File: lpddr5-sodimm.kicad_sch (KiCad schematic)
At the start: 0 parts

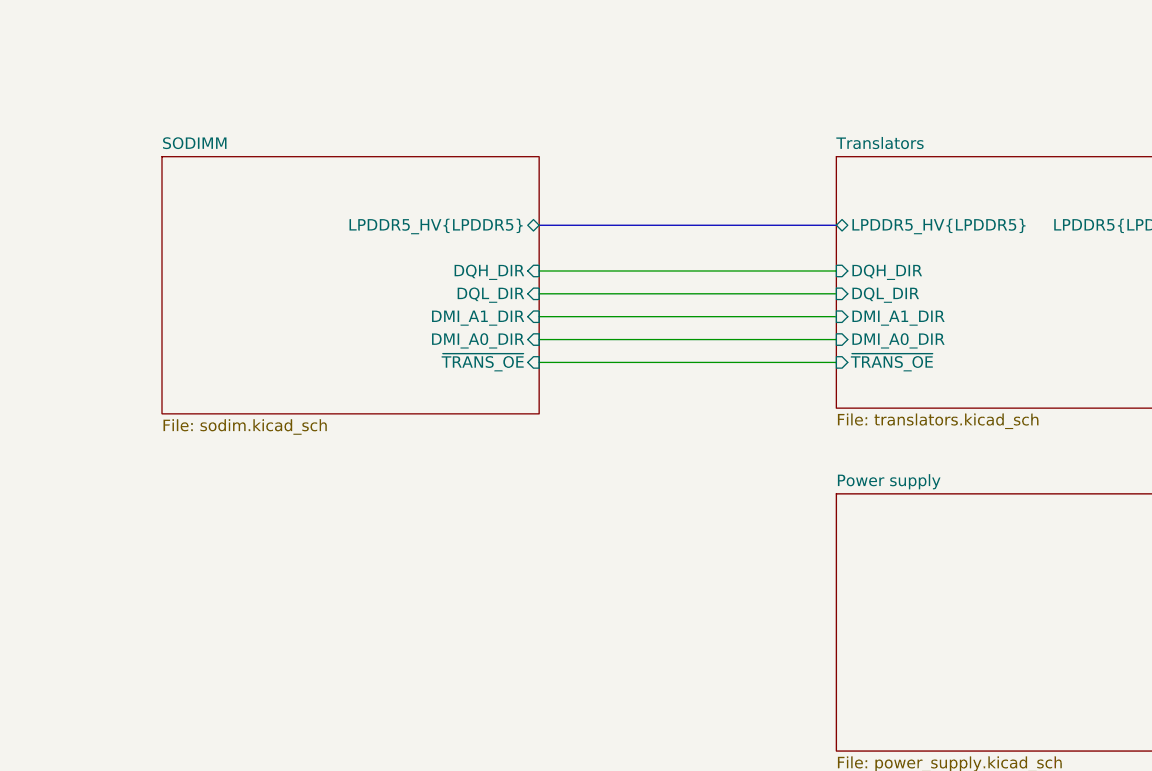
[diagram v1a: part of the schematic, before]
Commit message: [#52835] schematics: connect I2C on root sheet
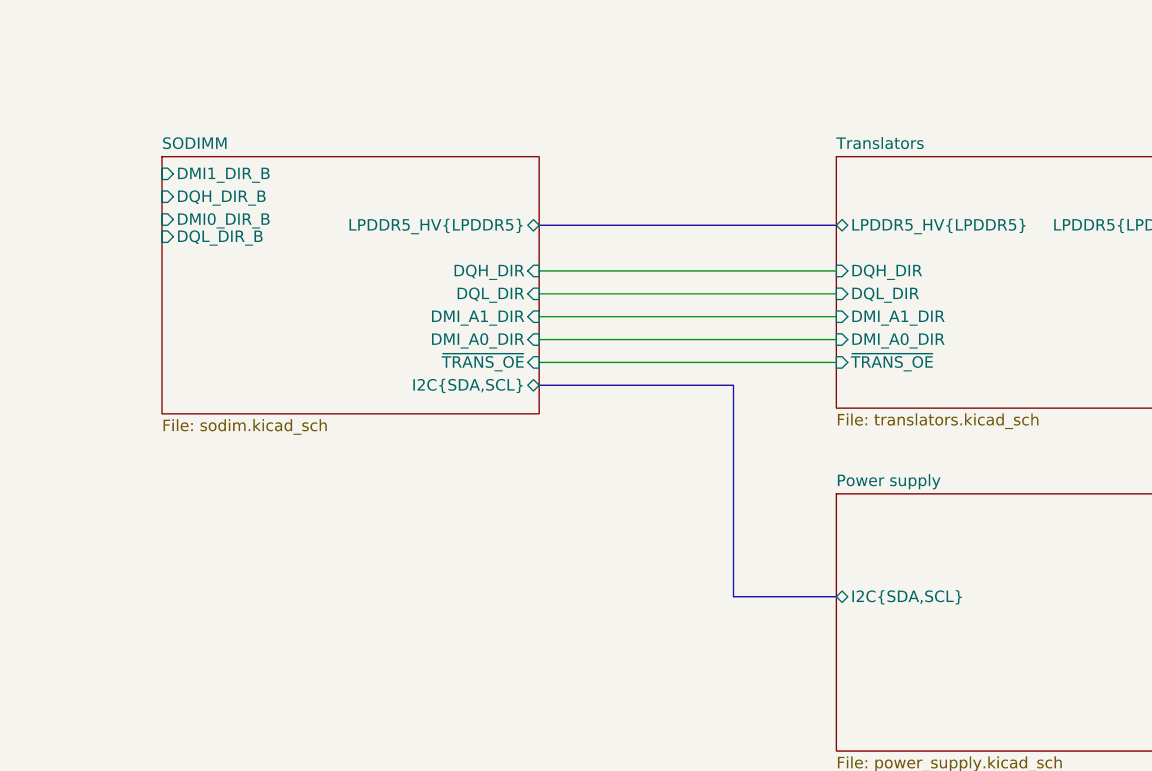
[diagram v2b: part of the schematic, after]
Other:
- sheet Power supply ports: added I2C{SDA,SCL}; removed none
- sheet SODIMM ports: added DMI0_DIR_B, DMI1_DIR_B, DQH_DIR_B, DQL_DIR_B, I2C{SDA,SCL}; removed none

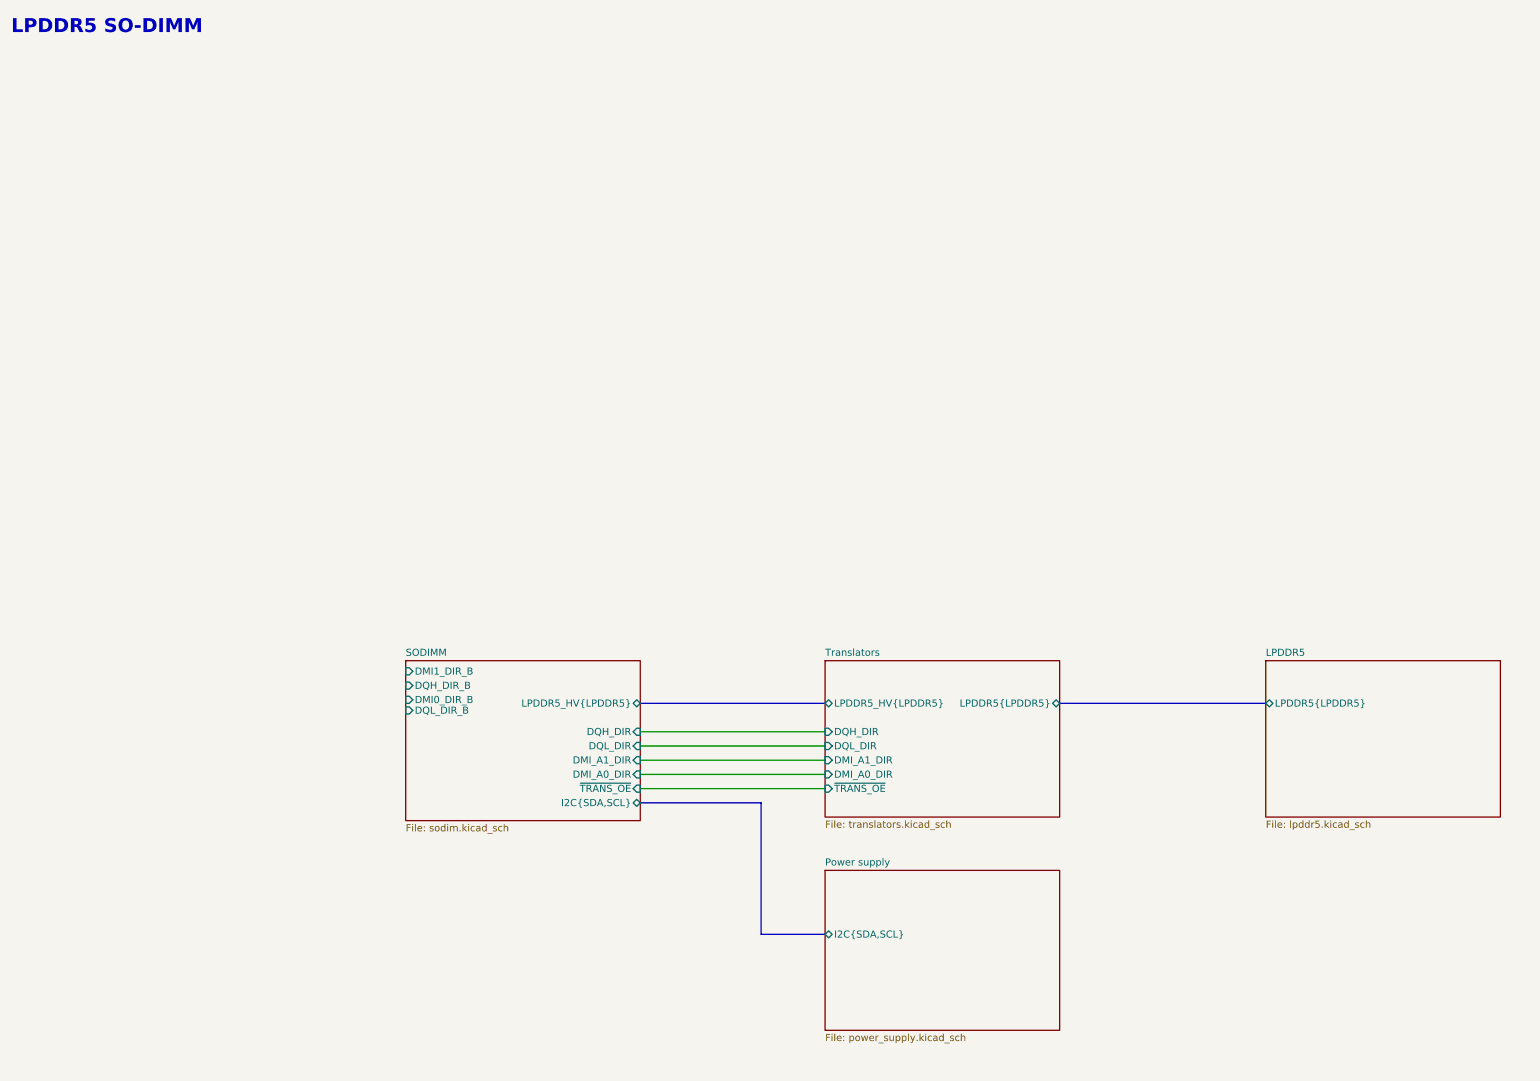
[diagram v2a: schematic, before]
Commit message: [#52835] schematics: update connections on root sheet
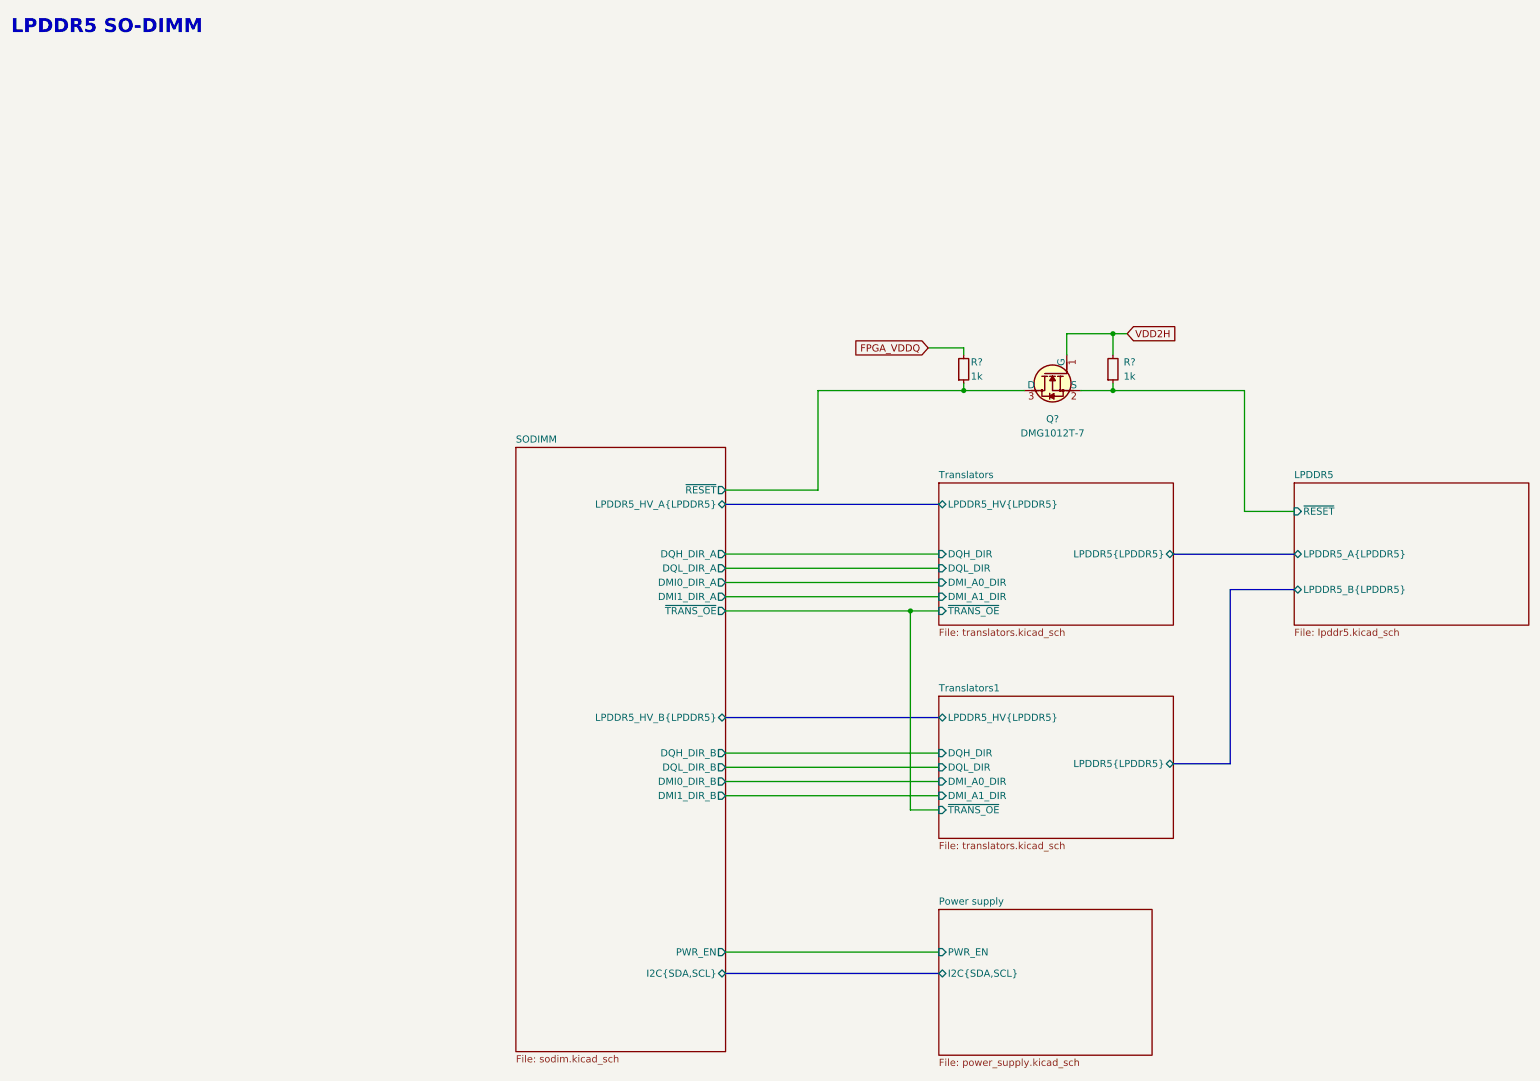
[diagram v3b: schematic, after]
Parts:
- added Q?: DMG1012T-7, antmicro-footprints:SOT-523, symbol antmicroTransistorsFETsMOSFETsSingle:DMG1012T-7
- added R? (x2): R_1k_0402, antmicro-footprints:R_0402_1005Metric, symbol antmicroResistors0402:R_1k_0402
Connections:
- new net FPGA_VDDQ: R?.2
- new net LPDDR5/~{RESET}: Q?.2 (S), R?.1
- new net SODIMM/~{RESET}: Q?.3 (D), R?.1
- new net VDD2H: Q?.1 (G), R?.2
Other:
- added sheet Translators1 (translators.kicad_sch)
- sheet LPDDR5 ports: added LPDDR5_A{LPDDR5}, LPDDR5_B{LPDDR5}, ~{RESET}; removed LPDDR5{LPDDR5}
- sheet Power supply ports: added PWR_EN; removed none
- sheet SODIMM ports: added DMI0_DIR_A, DMI1_DIR_A, DQH_DIR_A, DQL_DIR_A, LPDDR5_HV_A{LPDDR5}, LPDDR5_HV_B{LPDDR5}, PWR_EN, ~{RESET}; removed DMI_A0_DIR, DMI_A1_DIR, DQH_DIR, DQL_DIR, LPDDR5_HV{LPDDR5}

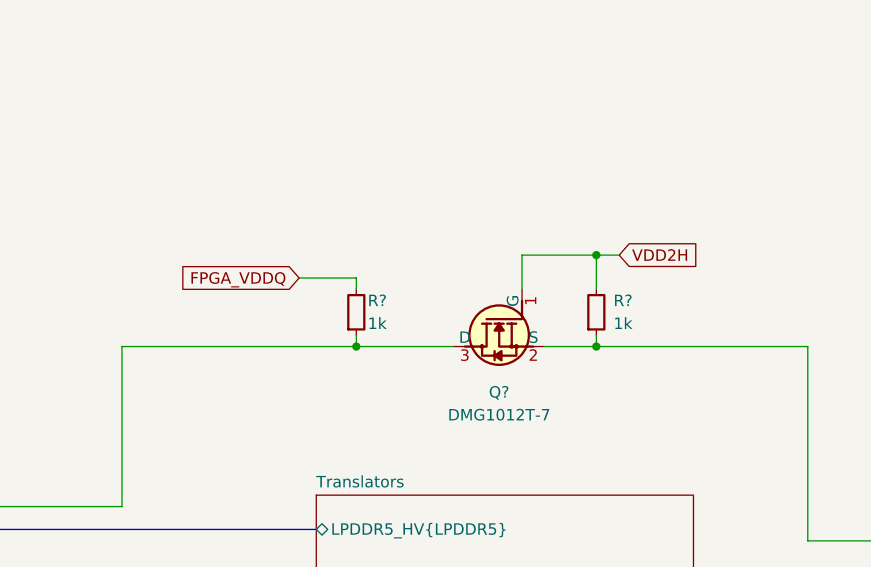
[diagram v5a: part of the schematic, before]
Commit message: [#52536] schematics: update I2C connection
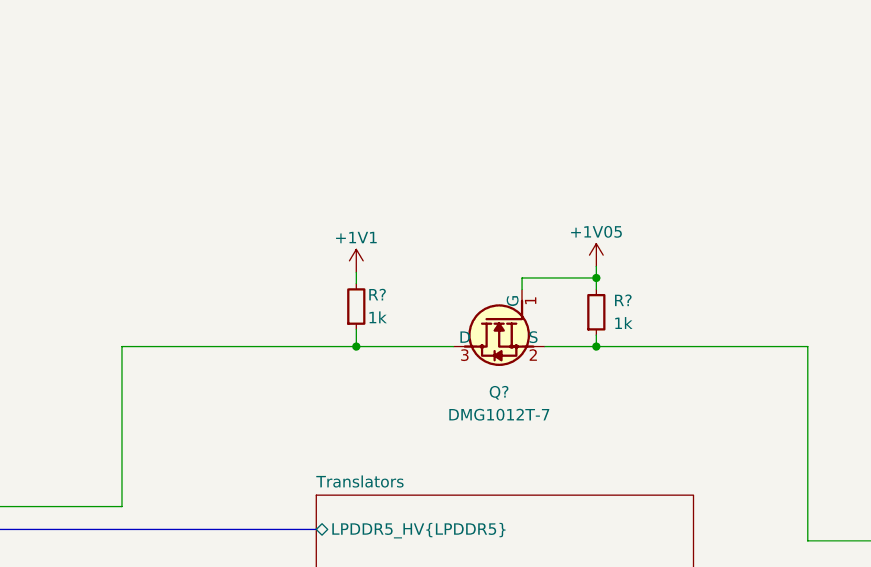
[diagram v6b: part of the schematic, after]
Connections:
- net FPGA_VDDQ renamed +1V1
- net VDD2H renamed +1V05
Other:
- moved on the sheet: R?

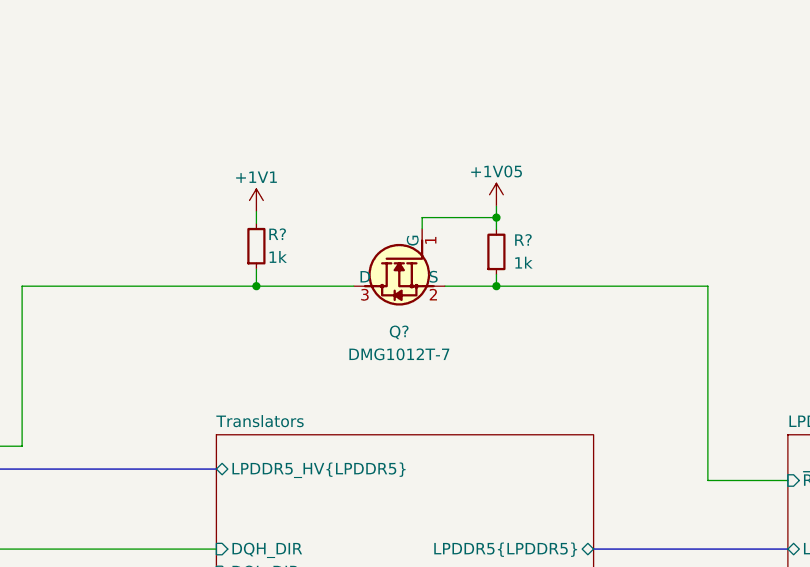
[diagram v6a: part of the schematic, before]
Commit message: [#52835] schematics: update components after standardization
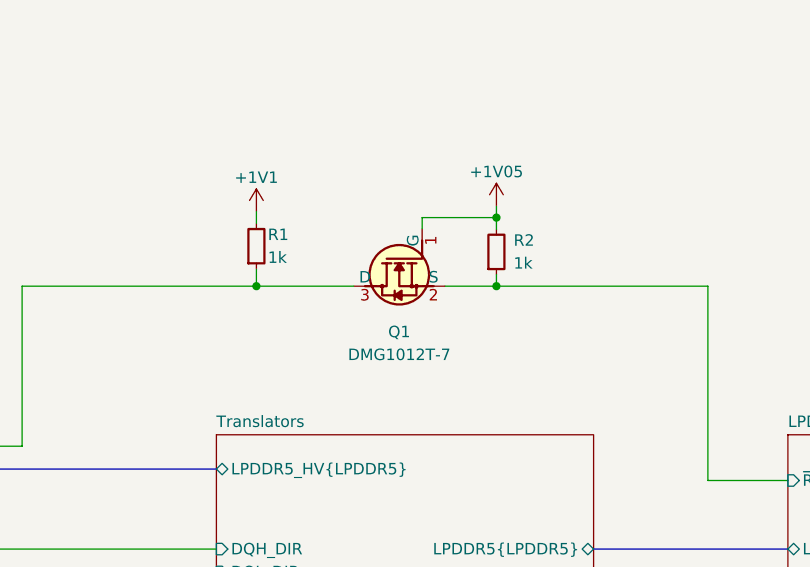
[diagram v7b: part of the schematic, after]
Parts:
- gave numbers to parts that had none: 3
